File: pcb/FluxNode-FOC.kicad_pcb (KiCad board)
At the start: 2 copper layers, 5 parts, among them IC1 DRV8323SRTAR, J1 XT60PW-F, J2 XT60PW-M, Q1 TPW1R306PL, U1 STM32G474RET6

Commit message: Unified all different LCSC part numbers of the same exact components to just one variant
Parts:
- removed Q1: TPW1R306PL, FluxNode-FOC:SOP_ADVANCE
- added C101: 100nF X7R 50V, FluxNode-FOC:C_0402_1005_DensityHigh, F.Cu at (369.8, 91.0)
- added C102: 100nF X7R 50V, FluxNode-FOC:C_0402_1005_DensityHigh, F.Cu at (369.8, 92.8)
- added C103: 22uF X7R 10V, FluxNode-FOC:C_0805_2012_DensityHigh, F.Cu at (363.1, 90.2)
- added C104: 2u2 X7R 100V, FluxNode-FOC:C_0805_2012_DensityHigh, F.Cu at (363.1, 82.0)
- added C105: 2u2 100V, FluxNode-FOC:C_0805_2012_DensityHigh, F.Cu at (363.1, 84.7)
- added C106: 2u2 100V, FluxNode-FOC:C_0805_2012_DensityHigh, F.Cu at (363.1, 87.5)
- added C107: 100nF 100V, FluxNode-FOC:C_0603_1608_DensityHigh, F.Cu at (366.8, 89.4)
- added C108: 2u2 100V, FluxNode-FOC:C_0805_2012_DensityHigh, F.Cu at (492.1, 81.5)
- added C109: 2u2 100V, FluxNode-FOC:C_0805_2012_DensityHigh, F.Cu at (492.1, 84.3)
- added C110: 10u 25V, FluxNode-FOC:C_0805_2012_DensityHigh, F.Cu at (492.1, 87.0)
- added C111: 22uF X7R 10V, FluxNode-FOC:C_0805_2012_DensityHigh, F.Cu at (492.1, 89.8)
- added C112: 1uF X7R 10V, FluxNode-FOC:C_0402_1005_DensityHigh, F.Cu at (369.8, 89.2)
- added C113: 100nF X7R 50V, FluxNode-FOC:C_0402_1005_DensityHigh, F.Cu at (491.5, 92.1)
- added C114: 15uF 25V, FluxNode-FOC:C_1210_3225_DensityHigh, F.Cu at (462.4, 106.5)
- added C115: 15uF 25V, FluxNode-FOC:C_1210_3225_DensityHigh, F.Cu at (462.4, 110.3)
- added C116: 2u2 X7R 100V, FluxNode-FOC:C_0805_2012_DensityHigh, F.Cu at (363.1, 93.0)
- added C117: 2u2 100V, FluxNode-FOC:C_0805_2012_DensityHigh, F.Cu at (363.1, 95.7)
- added C118: 4u7 100V, FluxNode-FOC:C_1206_3216_DensityHigh, F.Cu at (367.5, 82.5)
- added C119: 4u7 100V, FluxNode-FOC:C_1206_3216_DensityHigh, F.Cu at (367.5, 86.3)
- added C120: 220n 100V, FluxNode-FOC:C_0603_1608_DensityHigh, F.Cu at (366.8, 91.7)
- added C121: 220n 100V, FluxNode-FOC:C_0603_1608_DensityHigh, F.Cu at (366.8, 93.9)
- added C122: 1u 25V, FluxNode-FOC:C_0603_1608_DensityHigh, F.Cu at (486.8, 105.7)
- added C123: 10n 100V, FluxNode-FOC:C_0402_1005_DensityHigh, F.Cu at (491.5, 93.9)
- added C124: 4.7u 16V, FluxNode-FOC:C_0603_1608_DensityHigh, F.Cu at (486.8, 108.0)
- added C125: 1u X7R 10V, FluxNode-FOC:C_0402_1005_DensityHigh, F.Cu at (369.8, 94.6)
- added C126: 4.7u 100V, FluxNode-FOC:C_1206_3216_DensityHigh, F.Cu at (462.4, 81.7)
- added C127: 4.7u 100V, FluxNode-FOC:C_1206_3216_DensityHigh, F.Cu at (462.4, 84.8)
- added C128: 4.7u 100V, FluxNode-FOC:C_1206_3216_DensityHigh, F.Cu at (462.4, 87.8)
- added C129: 4.7u 100V, FluxNode-FOC:C_1206_3216_DensityHigh, F.Cu at (462.4, 90.8)
- added C130: 4.7u 100V, FluxNode-FOC:C_1206_3216_DensityHigh, F.Cu at (462.4, 93.9)
- added C131: 4.7u 100V, FluxNode-FOC:C_1206_3216_DensityHigh, F.Cu at (462.4, 97.0)
- added C132: 4.7u 100V, FluxNode-FOC:C_1206_3216_DensityHigh, F.Cu at (462.4, 100.0)
- added C133: 4.7u 100V, FluxNode-FOC:C_1206_3216_DensityHigh, F.Cu at (462.4, 103.0)
- added C134: 4.7u 100V, FluxNode-FOC:C_1206_3216_DensityHigh, F.Cu at (467.4, 81.7)
- added C135: 4.7u 100V, FluxNode-FOC:C_1206_3216_DensityHigh, F.Cu at (467.4, 84.8)
- added C136: 4.7u 100V, FluxNode-FOC:C_1206_3216_DensityHigh, F.Cu at (467.4, 87.8)
- added C137: 4.7u 100V, FluxNode-FOC:C_1206_3216_DensityHigh, F.Cu at (467.4, 90.8)
- added C138: 4.7u 100V, FluxNode-FOC:C_1206_3216_DensityHigh, F.Cu at (467.4, 93.9)
- added C139: 4.7u 100V, FluxNode-FOC:C_1206_3216_DensityHigh, F.Cu at (467.4, 97.0)
- added C140: 4.7u 100V, FluxNode-FOC:C_1206_3216_DensityHigh, F.Cu at (467.4, 100.0)
- added C141: 4.7u 100V, FluxNode-FOC:C_1206_3216_DensityHigh, F.Cu at (467.4, 103.0)
- added C142: 4.7u 100V, FluxNode-FOC:C_1206_3216_DensityHigh, F.Cu at (472.5, 81.7)
- added C143: 4.7u 100V, FluxNode-FOC:C_1206_3216_DensityHigh, F.Cu at (472.5, 84.8)
- added C144: 4.7u 100V, FluxNode-FOC:C_1206_3216_DensityHigh, F.Cu at (472.5, 87.8)
- added C145: 4.7u 100V, FluxNode-FOC:C_1206_3216_DensityHigh, F.Cu at (472.5, 90.8)
- added C146: 4.7u 100V, FluxNode-FOC:C_1206_3216_DensityHigh, F.Cu at (472.5, 93.9)
- added C147: 4.7u 100V, FluxNode-FOC:C_1206_3216_DensityHigh, F.Cu at (472.5, 97.0)
- added C148: 4.7u 100V, FluxNode-FOC:C_1206_3216_DensityHigh, F.Cu at (472.5, 100.0)
- added C149: 4.7u 100V, FluxNode-FOC:C_1206_3216_DensityHigh, F.Cu at (472.5, 103.0)
- added C150: 4.7u 100V, FluxNode-FOC:C_1206_3216_DensityHigh, F.Cu at (477.6, 81.7)
- added C151: 4.7u 100V, FluxNode-FOC:C_1206_3216_DensityHigh, F.Cu at (477.6, 84.8)
- added C152: 4.7u 100V, FluxNode-FOC:C_1206_3216_DensityHigh, F.Cu at (477.6, 87.8)
- added C153: 4.7u 100V, FluxNode-FOC:C_1206_3216_DensityHigh, F.Cu at (477.6, 90.8)
- added C154: 4.7u 100V, FluxNode-FOC:C_1206_3216_DensityHigh, F.Cu at (477.6, 93.9)
- added C155: 4.7u 100V, FluxNode-FOC:C_1206_3216_DensityHigh, F.Cu at (477.6, 97.0)
- added C156: 4.7u 100V, FluxNode-FOC:C_1206_3216_DensityHigh, F.Cu at (477.6, 100.0)
- added C157: 4.7u 100V, FluxNode-FOC:C_1206_3216_DensityHigh, F.Cu at (477.6, 103.0)
- added C158: 4.7u 100V, FluxNode-FOC:C_1206_3216_DensityHigh, F.Cu at (482.6, 81.7)
- added C159: 4.7u 100V, FluxNode-FOC:C_1206_3216_DensityHigh, F.Cu at (482.6, 84.8)
- added C160: 4.7u 100V, FluxNode-FOC:C_1206_3216_DensityHigh, F.Cu at (482.6, 87.8)
- added C161: 4.7u 100V, FluxNode-FOC:C_1206_3216_DensityHigh, F.Cu at (482.6, 90.8)
- added C162: 4.7u 100V, FluxNode-FOC:C_1206_3216_DensityHigh, F.Cu at (482.6, 93.9)
- added C163: 4.7u 100V, FluxNode-FOC:C_1206_3216_DensityHigh, F.Cu at (482.6, 97.0)
- added C164: 4.7u 100V, FluxNode-FOC:C_1206_3216_DensityHigh, F.Cu at (482.6, 100.0)
- added C165: 4.7u 100V, FluxNode-FOC:C_1206_3216_DensityHigh, F.Cu at (482.6, 103.0)
- added C166: 4.7u 100V, FluxNode-FOC:C_1206_3216_DensityHigh, F.Cu at (487.6, 81.7)
- added C167: 4.7u 100V, FluxNode-FOC:C_1206_3216_DensityHigh, F.Cu at (487.6, 84.8)
- added C168: 4.7u 100V, FluxNode-FOC:C_1206_3216_DensityHigh, F.Cu at (487.6, 87.8)
- added C169: 4.7u 100V, FluxNode-FOC:C_1206_3216_DensityHigh, F.Cu at (487.6, 90.8)
- added C170: 4.7u 100V, FluxNode-FOC:C_1206_3216_DensityHigh, F.Cu at (487.6, 93.9)
- added C171: 4.7u 100V, FluxNode-FOC:C_1206_3216_DensityHigh, F.Cu at (487.6, 97.0)
- added C172: 4.7u 100V, FluxNode-FOC:C_1206_3216_DensityHigh, F.Cu at (487.6, 100.0)
- added C173: 4.7u 100V, FluxNode-FOC:C_1206_3216_DensityHigh, F.Cu at (487.6, 103.0)
- added C201: 1uF X7R 10V, FluxNode-FOC:C_0402_1005_DensityHigh, F.Cu at (444.2, 37.3)
- added C202: 100n 50V, FluxNode-FOC:C_0402_1005_DensityHigh, F.Cu at (444.2, 39.1)
- added C203: 100n 50V, FluxNode-FOC:C_0402_1005_DensityHigh, F.Cu at (444.2, 40.9)
- added C204: 100n 50V, FluxNode-FOC:C_0402_1005_DensityHigh, F.Cu at (444.2, 42.7)
- added C205: 100n 50V, FluxNode-FOC:C_0402_1005_DensityHigh, F.Cu at (444.2, 44.5)
- added C206: 4.7u 16V, FluxNode-FOC:C_0603_1608_DensityHigh, F.Cu at (449.8, 40.0)
- added C207: 1uF 10V, FluxNode-FOC:C_0402_1005_DensityHigh, F.Cu at (446.8, 37.3)
- added C208: 100n 50V, FluxNode-FOC:C_0402_1005_DensityHigh, F.Cu at (446.8, 39.1)
- added C209: 1uF X7R 10V, FluxNode-FOC:C_0402_1005_DensityHigh, F.Cu at (446.8, 40.9)
- added C210: 100n 50V, FluxNode-FOC:C_0402_1005_DensityHigh, F.Cu at (446.8, 42.7)
- added C211: 4.7u X5R 25V, FluxNode-FOC:C_0402_1005_DensityHigh, F.Cu at (446.8, 44.5)
- added C212: 1nF 25V, FluxNode-FOC:C_0402_1005_DensityHigh, F.Cu at (339.0, 138.9)
- added C213: 1nF 25V, FluxNode-FOC:C_0402_1005_DensityHigh, F.Cu at (339.0, 140.7)
- added C214: 1nF 25V, FluxNode-FOC:C_0402_1005_DensityHigh, F.Cu at (339.0, 142.5)
- added C215: 470pF 50V, FluxNode-FOC:C_0402_1005_DensityHigh, F.Cu at (365.4, -21.0)
- added C216: 470pF 50V, FluxNode-FOC:C_0402_1005_DensityHigh, F.Cu at (365.4, -19.2)
- added C217: 470pF 50V, FluxNode-FOC:C_0402_1005_DensityHigh, F.Cu at (365.4, -17.4)
- added C301: 1u 25V, FluxNode-FOC:C_0603_1608_DensityHigh, F.Cu at (490.2, 61.9)
- added C302: 4u7 100V, FluxNode-FOC:C_1206_3216_DensityHigh, F.Cu at (491.0, 59.2)
- added C303: 100nF 100V, FluxNode-FOC:C_0603_1608_DensityHigh, F.Cu at (490.2, 64.1)
- added C308: 100nF 50V, FluxNode-FOC:C_0402_1005_DensityHigh, F.Cu at (198.2, 45.1)
- added C309: 1uF 50V, FluxNode-FOC:C_0603_1608_DensityHigh, F.Cu at (125.5, 179.9)
- added C401: 100n 50V, FluxNode-FOC:C_0402_1005_DensityHigh, F.Cu at (268.2, 131.8)
- added C501: 100nF, FluxNode-FOC:C_0402_1005_DensityHigh, F.Cu at (318.8, 138.9)
- added C502: 100nF, FluxNode-FOC:C_0402_1005_DensityHigh, F.Cu at (318.8, 140.7)
- added C503: 100nF 50V, FluxNode-FOC:C_0402_1005_DensityHigh, F.Cu at (318.8, 142.5)
- added C504: 100nF 50V, FluxNode-FOC:C_0402_1005_DensityHigh, F.Cu at (318.8, 144.3)
- added C701: 1nF 1kV, FluxNode-FOC:C_0603_1608_DensityHigh, F.Cu at (256.0, 139.1)
- added C702: 1nF 1kV, FluxNode-FOC:C_0603_1608_DensityHigh, F.Cu at (256.0, 141.4)
- added C703: 1nF 1kV, FluxNode-FOC:C_0603_1608_DensityHigh, F.Cu at (256.0, 143.6)
- added C704: 1nF 1kV, FluxNode-FOC:C_0603_1608_DensityHigh, F.Cu at (256.0, 145.9)
- added C801: 3n3 10% 100V, FluxNode-FOC:C_0402_1005_DensityHigh, F.Cu at (357.1, -3.63)
- added C802: 3n3 10% 100V, FluxNode-FOC:C_0402_1005_DensityHigh, F.Cu at (357.1, -1.83)
- added C803: 4.7u 100V, FluxNode-FOC:C_1206_3216_DensityHigh, F.Cu at (339.8, -11.9)
- added C804: 100nF 100V, FluxNode-FOC:C_1206_3216_DensityHigh, F.Cu at (339.8, -8.80)
- added C805: 3n3 10% 100V, FluxNode-FOC:C_0402_1005_DensityHigh, F.Cu at (357.1, -0.03)
- added C806: 3n3 10% 100V, FluxNode-FOC:C_0402_1005_DensityHigh, F.Cu at (357.1, 1.77)
- added C807: 100nF 100V, FluxNode-FOC:C_1206_3216_DensityHigh, F.Cu at (339.8, -5.75)
- added C808: 4.7u 100V, FluxNode-FOC:C_1206_3216_DensityHigh, F.Cu at (339.8, -2.71)
- added C809: 3n3 10% 100V, FluxNode-FOC:C_0402_1005_DensityHigh, F.Cu at (357.1, 3.57)
- added C810: 3n3 10% 100V, FluxNode-FOC:C_0402_1005_DensityHigh, F.Cu at (357.1, 5.37)
- added C811: 100nF 100V, FluxNode-FOC:C_1206_3216_DensityHigh, F.Cu at (339.8, 0.34)
- added C812: 4.7u 100V, FluxNode-FOC:C_1206_3216_DensityHigh, F.Cu at (339.8, 3.40)
- added D101: SMBJ51CD-M3_H, FluxNode-FOC:DIOM4336X24N, F.Cu at (433.9, 90.5)
- added D102: SMBJ51CD-M3_H, FluxNode-FOC:DIOM4336X24N, F.Cu at (433.9, 95.5)
- added D501: PESD4USB3U-TBSX, FluxNode-FOC:PESD4USB3UTBSX, F.Cu at (328.1, 150.3)
- added D801: BAT41ZFILM, FluxNode-FOC:SOD3816X145N, F.Cu at (334.4, -20.0)
- added D802: BAT41ZFILM, FluxNode-FOC:SOD3816X145N, F.Cu at (334.4, -16.7)
- added D803: BAT41ZFILM, FluxNode-FOC:SOD3816X145N, F.Cu at (334.4, -13.4)
- added D804: BAT41ZFILM, FluxNode-FOC:SOD3816X145N, F.Cu at (334.4, -10.2)
- added D805: BAT41ZFILM, FluxNode-FOC:SOD3816X145N, F.Cu at (334.4, -6.88)
- added D806: BAT41ZFILM, FluxNode-FOC:SOD3816X145N, F.Cu at (334.4, -3.60)
- added D807: BAT41ZFILM, FluxNode-FOC:SOD3816X145N, F.Cu at (334.4, -0.32)
- added D808: BAT41ZFILM, FluxNode-FOC:SOD3816X145N, F.Cu at (334.4, 2.96)
- added D809: BAT41ZFILM, FluxNode-FOC:SOD3816X145N, F.Cu at (334.4, 6.24)
- added FB101: 1k @ 100MHz, FluxNode-FOC:R_0805_2012_DensityHigh, F.Cu at (466.8, 105.8)
- added FB102: 1k @ 100MHz, FluxNode-FOC:R_0805_2012_DensityHigh, F.Cu at (466.8, 111.0)
- added FB103: 1k @ 100MHz, FluxNode-FOC:R_0805_2012_DensityHigh, F.Cu at (466.8, 108.4)
- added FB201: 1k @ 100MHz, FluxNode-FOC:R_0805_2012_DensityHigh, F.Cu at (450.0, 37.6)
- added FID701: Fiducial, Fiducial:Fiducial_1mm_Mask2mm, F.Cu at (256.0, 132.7)
- added FID702: Fiducial, Fiducial:Fiducial_1mm_Mask2mm, F.Cu at (256.0, 136.2)
- added FID703: Fiducial, Fiducial:Fiducial_1mm_Mask2mm, F.Cu at (259.6, 132.7)
- added FID704: Fiducial, Fiducial:Fiducial_1mm_Mask2mm, F.Cu at (259.6, 136.2)
- added FID705: Fiducial, Fiducial:Fiducial_1mm_Mask2mm, F.Cu at (263.1, 132.7)
- added FID706: Fiducial, Fiducial:Fiducial_1mm_Mask2mm, F.Cu at (263.1, 136.2)
- added H701: MountingHole_Pad, MountingHole:MountingHole_3.2mm_M3_Pad_Via, F.Cu at (250.3, 134.9)
- added H702: MountingHole_Pad, MountingHole:MountingHole_3.2mm_M3_Pad_Via, F.Cu at (250.3, 142.8)
- added H703: MountingHole_Pad, MountingHole:MountingHole_3.2mm_M3_Pad_Via, F.Cu at (250.3, 150.8)
- added H704: MountingHole_Pad, MountingHole:MountingHole_3.2mm_M3_Pad_Via, F.Cu at (250.3, 158.7)
- added J501: XT30PW_2_2_-M.G.B, FluxNode-FOC:AMASS_XT30PW_2_2_-M.G.B, F.Cu at (164.7, 164.9)
- added J502: Conn_01x08_Pin, Connector_JST:JST_GH_SM08B-GHS-TB_1x08-1MP_P1.25mm_Horizontal, F.Cu at (70.9, 127.5)
- added J503: TYPE-C-31-M-12, FluxNode-FOC:HRO_TYPE-C-31-M-12, F.Cu at (326.2, 144.7)
- added L101: 22uH 830mA 360mOhms, FluxNode-FOC:L_Coilcraft_LPS4018, F.Cu at (373.0, 83.3)
- added L102: 2.2uH 1,2A 100mOhms, FluxNode-FOC:L_Coilcraft_LPS3314, F.Cu at (477.2, 107.2)
- added L103: 22uH 830mA 360mOhms, FluxNode-FOC:L_Coilcraft_LPS4018, F.Cu at (471.6, 107.3)
- added Q301: TPW1R306PL, FluxNode-FOC:SOP_ADVANCE, F.Cu at (151.7, 167.1)
- added Q801: TPW1R306PL, FluxNode-FOC:SOP_ADVANCE, F.Cu at (385.1, 109.8)
- added Q802: TPW1R306PL, FluxNode-FOC:SOP_ADVANCE, F.Cu at (391.2, 109.8)
- added Q803: TPW1R306PL, FluxNode-FOC:SOP_ADVANCE, F.Cu at (340.4, -17.9)
- added Q804: TPW1R306PL, FluxNode-FOC:SOP_ADVANCE, F.Cu at (346.6, -17.9)
- added Q805: TPW1R306PL, FluxNode-FOC:SOP_ADVANCE, F.Cu at (352.8, -17.9)
- added Q806: TPW1R306PL, FluxNode-FOC:SOP_ADVANCE, F.Cu at (359.0, -17.9)
- added R101: 10k 1% 50V, FluxNode-FOC:R_0402_1005_DensityHigh, F.Cu at (368.0, 63.3)
- added R102: 0R, FluxNode-FOC:R_0402_1005_DensityHigh, F.Cu at (368.0, 61.5)
- added R103: 100k 1% 50V, FluxNode-FOC:R_0402_1005_DensityHigh, F.Cu at (368.0, 65.1)
- added R104: 9.09k 1% 50V, FluxNode-FOC:R_0402_1005_DensityHigh, F.Cu at (491.5, 101.1)
- added R201: 22R 1%, FluxNode-FOC:R_0402_1005_DensityHigh, F.Cu at (339.0, 144.3)
- added R202: 22R 1%, FluxNode-FOC:R_0402_1005_DensityHigh, F.Cu at (339.0, 146.1)
- added R203: 22R 1%, FluxNode-FOC:R_0402_1005_DensityHigh, F.Cu at (339.0, 147.9)
- added R204: 22R 1%, FluxNode-FOC:R_0402_1005_DensityHigh, F.Cu at (339.0, 149.7)
- added R205: 22R 1%, FluxNode-FOC:R_0402_1005_DensityHigh, F.Cu at (339.0, 151.5)
- added R206: 1K 1%, FluxNode-FOC:R_0402_1005_DensityHigh, F.Cu at (365.4, -15.6)
- added R207: 1K 1%, FluxNode-FOC:R_0402_1005_DensityHigh, F.Cu at (365.4, -13.8)
- added R208: 1K 1%, FluxNode-FOC:R_0402_1005_DensityHigh, F.Cu at (365.4, -12.0)
- added R304: 100, FluxNode-FOC:R_0402_1005_DensityHigh, F.Cu at (198.2, 46.9)
- added R305: 10k, FluxNode-FOC:R_0402_1005_DensityHigh, F.Cu at (198.2, 48.7)
- added R306: 4.7, FluxNode-FOC:R_0603_1608_DensityHigh, F.Cu at (153.7, 171.9)
- added R307: 1.5, FluxNode-FOC:R_0603_1608_DensityHigh, F.Cu at (152.4, 171.9)
- added R308: 47k, FluxNode-FOC:R_0402_1005_DensityHigh, F.Cu at (198.2, 50.5)
- added R401: 100k 1%, FluxNode-FOC:R_0402_1005_DensityHigh, F.Cu at (268.2, 133.6)
- added R402: 8k2 1%, FluxNode-FOC:R_0402_1005_DensityHigh, F.Cu at (268.2, 135.4)
- added R501: 5k1 1%, FluxNode-FOC:R_0402_1005_DensityHigh, F.Cu at (318.8, 146.1)
- added R502: 5k1 1%, FluxNode-FOC:R_0402_1005_DensityHigh, F.Cu at (318.8, 147.9)
- added R503: 100k, FluxNode-FOC:R_0402_1005_DensityHigh, F.Cu at (318.8, 149.7)
- added R504: 100k, FluxNode-FOC:R_0402_1005_DensityHigh, F.Cu at (318.8, 151.5)
- added R701: 0R, FluxNode-FOC:R_0603_1608_DensityHigh, F.Cu at (259.3, 139.1)
- added R702: 0R, FluxNode-FOC:R_0603_1608_DensityHigh, F.Cu at (259.3, 141.2)
- added R703: 0R, FluxNode-FOC:R_0603_1608_DensityHigh, F.Cu at (259.3, 143.4)
- added R704: 0R, FluxNode-FOC:R_0603_1608_DensityHigh, F.Cu at (259.3, 145.5)
- added R801: 7.5 1% 0.5W, FluxNode-FOC:R_0805_2012_DensityHigh, F.Cu at (353.9, -12.1)
- added R802: 7.5 1% 0.5W, FluxNode-FOC:R_0805_2012_DensityHigh, F.Cu at (353.9, -9.55)
- added R803: 5R 1% 0.4W, FluxNode-FOC:R_0603_1608_DensityHigh, F.Cu at (343.9, -12.3)
- added R804: 5R 1% 0.4W, FluxNode-FOC:R_0603_1608_DensityHigh, F.Cu at (343.9, -10.2)
- added R805: 0.5m 1% 2W, FluxNode-FOC:R_1206_3216_DensityHigh, F.Cu at (358.2, -11.9)
- added R806: 43k 1% 75V, FluxNode-FOC:R_0603_1608_DensityHigh, F.Cu at (343.9, -8.01)
- added R807: 43k 1% 75V, FluxNode-FOC:R_0603_1608_DensityHigh, F.Cu at (343.9, -5.86)
- added R808: 6k8 1% 75V, FluxNode-FOC:R_0603_1608_DensityHigh, F.Cu at (343.9, -3.71)
- added R809: 43k 1% 75V, FluxNode-FOC:R_0603_1608_DensityHigh, F.Cu at (343.9, -1.55)
- added R810: 43k 1% 75V, FluxNode-FOC:R_0603_1608_DensityHigh, F.Cu at (347.1, -12.3)
- added R811: 6k8 1% 75V, FluxNode-FOC:R_0603_1608_DensityHigh, F.Cu at (347.1, -10.2)
- added R812: 43k 1% 75V, FluxNode-FOC:R_0603_1608_DensityHigh, F.Cu at (347.1, -8.01)
- added R813: 43k 1% 75V, FluxNode-FOC:R_0603_1608_DensityHigh, F.Cu at (347.1, -5.86)
- added R814: 6k8 1% 75V, FluxNode-FOC:R_0603_1608_DensityHigh, F.Cu at (347.1, -3.71)
- added R815: 7.5 1% 0.5W, FluxNode-FOC:R_0805_2012_DensityHigh, F.Cu at (353.9, -7.00)
- added R816: 7.5 1% 0.5W, FluxNode-FOC:R_0805_2012_DensityHigh, F.Cu at (353.9, -4.46)
- added R817: 0.5m 1% 2W, FluxNode-FOC:R_1206_3216_DensityHigh, F.Cu at (358.2, -8.96)
- added R818: 5R 1% 0.4W, FluxNode-FOC:R_0603_1608_DensityHigh, F.Cu at (347.1, -1.55)
- added R819: 5R 1% 0.4W, FluxNode-FOC:R_0603_1608_DensityHigh, F.Cu at (350.4, -12.3)
- added R820: 7.5 1% 0.5W, FluxNode-FOC:R_0805_2012_DensityHigh, F.Cu at (353.9, -1.91)
- added R821: 7.5 1% 0.5W, FluxNode-FOC:R_0805_2012_DensityHigh, F.Cu at (353.9, 0.65)
- added R822: 0.5m 1% 2W, FluxNode-FOC:R_1206_3216_DensityHigh, F.Cu at (358.2, -6.00)
- added R823: 5R 1% 0.4W, FluxNode-FOC:R_0603_1608_DensityHigh, F.Cu at (350.4, -10.2)
- added R824: 5R 1% 0.4W, FluxNode-FOC:R_0603_1608_DensityHigh, F.Cu at (350.4, -8.01)
- added U101: TPS62172DSG, Package_SON:WSON-8-1EP_2x2mm_P0.5mm_EP0.9x1.6mm_ThermalVias, F.Cu at (490.7, 106.5)
- added U102: LMR36506MSC5RPERQ1, FluxNode-FOC:LMR36503, F.Cu at (373.0, 94.9)
- added U103: LP2992IM5-3.3/NOPB, Package_TO_SOT_SMD:SOT-23-5, F.Cu at (482.4, 107.0)
- added U104: LMR36006FSCQ, FluxNode-FOC:LMR36006, F.Cu at (372.9, 90.6)
- added U301: UCC27511ADBV, Package_TO_SOT_SMD:SOT-23-6, F.Cu at (153.3, 175.2)
- added U501: USBLC6-2SC6, Package_TO_SOT_SMD:SOT-23-6, F.Cu at (322.7, 150.5)
- moved IC1 255.8 mm to (386.6, 56.4)
- moved U201 251.8 mm to (386.5, 69.6)
- moved J102 5.83 mm to (104.4, 69.7)
- moved J101 5.50 mm to (95.3, 69.7)
- renumbered J1 to J101, J2 to J102, U1 to U201
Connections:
- net /03-Motor-Driver/SHA renamed /03 Motor Control - Gate Driver/SHA
- net /03-Motor-Driver/SHB renamed /03 Motor Control - Gate Driver/SHB
- net /03-Motor-Driver/SHC renamed /03 Motor Control - Gate Driver/SHC
- net /03-Motor-Driver/SNA renamed /03 Motor Control - Gate Driver/SNA
- net /03-Motor-Driver/SNB renamed /03 Motor Control - Gate Driver/SNB
- net /03-Motor-Driver/SNC renamed /03 Motor Control - Gate Driver/SNC
- net /03-Motor-Driver/SPA renamed /03 Motor Control - Gate Driver/SPA
- net /03-Motor-Driver/SPB renamed /03 Motor Control - Gate Driver/SPB
- net /03-Motor-Driver/SPC renamed /03 Motor Control - Gate Driver/SPC
- IC1 pad 1: unconnected-(IC1-CPL-Pad1) -> Net-(IC1-CPL)
- IC1 pad 13: /03-Motor-Driver/GLB -> /03 Motor Control - Gate Driver/GLB
- IC1 pad 15: /03-Motor-Driver/GHB -> /03 Motor Control - Gate Driver/GHB
- IC1 pad 16: /03-Motor-Driver/GHC -> /03 Motor Control - Gate Driver/GHC
- IC1 pad 18: /03-Motor-Driver/GLC -> /03 Motor Control - Gate Driver/GLC
- IC1 pad 2: unconnected-(IC1-CPH-Pad2) -> Net-(IC1-CPH)
- IC1 pad 21: /03-Motor-Driver/SOC -> /02 MCU/SOC
- IC1 pad 22: /03-Motor-Driver/SOB -> /02 MCU/SOB
- IC1 pad 23: /03-Motor-Driver/SOA -> /02 MCU/SOA
- IC1 pad 24: /03-Motor-Driver/VREF -> +A3V3
- IC1 pad 25: /03-Motor-Driver/nFault -> /02 MCU/DRV_nFAULT
- IC1 pad 26: /03-Motor-Driver/SDO -> /02 MCU/SPI1_MISO
- IC1 pad 27: /03-Motor-Driver/SDI -> /02 MCU/SPI1_MOSI
- IC1 pad 28: /03-Motor-Driver/SCLK -> /02 MCU/SPI1_SCK
- IC1 pad 29: /03-Motor-Driver/nSCS -> /02 MCU/SPI1_DRV_CS
- IC1 pad 3: unconnected-(IC1-VCP-Pad3) -> Net-(IC1-VCP)
- IC1 pad 30: /03-Motor-Driver/EN -> /02 MCU/DRV_EN
- IC1 pad 31: /03-Motor-Driver/CAL -> /02 MCU/DRV_CAL
- IC1 pad 32: unconnected-(IC1-AGND-Pad32) -> GND
- IC1 pad 33: unconnected-(IC1-DVDD-Pad33) -> Net-(IC1-DVDD)
- IC1 pad 34: /03-Motor-Driver/INHA -> /02 MCU/DRV_PWM_HA
- IC1 pad 35: /03-Motor-Driver/INLA -> /02 MCU/DRV_PWM_LA
- IC1 pad 36: /03-Motor-Driver/INHB -> /02 MCU/DRV_PWM_HB
- IC1 pad 37: /03-Motor-Driver/INLB -> /02 MCU/DRV_PWM_LB
- IC1 pad 38: /03-Motor-Driver/INHC -> /02 MCU/DRV_PWM_HC
- IC1 pad 39: /03-Motor-Driver/INLC -> /02 MCU/DRV_PWM_LC
- IC1 pad 4: unconnected-(IC1-VM-Pad4) -> +VBAT
- IC1 pad 40: unconnected-(IC1-PGND-Pad40) -> GND
- IC1 pad 41: unconnected-(IC1-EP-Pad41) -> GND
- IC1 pad 5: unconnected-(IC1-VDRAIN-Pad5) -> +VBAT
- IC1 pad 6: /03-Motor-Driver/GHA -> /03 Motor Control - Gate Driver/GHA
- IC1 pad 8: /03-Motor-Driver/GLA -> /03 Motor Control - Gate Driver/GLA
- J101 pad 2: /01-Power/+VBAT -> +VBAT
- J102 pad 2: /01-Power/+VBAT -> +VBAT
- U201 pad 1: unconnected-(U1-VBAT-Pad1) -> +3V3
- U201 pad 10: unconnected-(U1-PC2-Pad10) -> /02 MCU/DRV_PWM_HA
- U201 pad 11: unconnected-(U1-PC3-Pad11) -> /02 MCU/SENSE_UA
- U201 pad 12: unconnected-(U1-PA0-Pad12) -> /02 MCU/SENSE_UC
- U201 pad 13: unconnected-(U1-PA1-Pad13) -> /02 MCU/SENSE_UB
- U201 pad 14: unconnected-(U1-PA2-Pad14) -> /02 MCU/DRV_CAL
- U201 pad 15: Net-(U1-VSS-Pad15) -> GND
- U201 pad 16: unconnected-(U1-VDD-Pad16) -> +3V3
- U201 pad 17: unconnected-(U1-PA3-Pad17) -> /02 MCU/DRV_EN
- U201 pad 18: unconnected-(U1-PA4-Pad18) -> /02 MCU/SPI1_DRV_CS
- U201 pad 19: unconnected-(U1-PA5-Pad19) -> /02 MCU/SPI1_SCK
- U201 pad 2: unconnected-(U1-PC13-Pad2) -> /02 MCU/DRV_PWM_LC
- U201 pad 20: unconnected-(U1-PA6-Pad20) -> /02 MCU/SPI1_MISO
- U201 pad 21: unconnected-(U1-PA7-Pad21) -> /02 MCU/SPI1_MOSI
- U201 pad 22: unconnected-(U1-PC4-Pad22) -> /02 MCU/DRV_nFAULT
- U201 pad 23: unconnected-(U1-PC5-Pad23) -> /02 MCU/SPI1_MAG_CS
- U201 pad 24: unconnected-(U1-PB0-Pad24) -> /02 MCU/DRV_SOA_FILT
- U201 pad 25: unconnected-(U1-PB1-Pad25) -> /02 MCU/DRV_SOB_FILT
- U201 pad 26: unconnected-(U1-PB2-Pad26) -> /02 MCU/DRV_SOC_FILT
- U201 pad 27: unconnected-(U1-VSSA-Pad27) -> GND
- U201 pad 28: unconnected-(U1-VREF+-Pad28) -> /02 MCU/F_A3V3
- U201 pad 29: unconnected-(U1-VDDA-Pad29) -> /02 MCU/F_A3V3
- U201 pad 31: Net-(U1-VSS-Pad15) -> GND
- U201 pad 32: unconnected-(U1-VDD-Pad32) -> +3V3
- U201 pad 33: unconnected-(U1-PB11-Pad33) -> /02 MCU/FAN_CTRL
- U201 pad 34: unconnected-(U1-PB12-Pad34) -> /02 MCU/SENSE_TEMP_BRAKE
- U201 pad 35: unconnected-(U1-PB13-Pad35) -> /02 MCU/SENSE_VBAT
- U201 pad 36: unconnected-(U1-PB14-Pad36) -> /02 MCU/DRV_PWM_LB
- U201 pad 37: unconnected-(U1-PB15-Pad37) -> /02 MCU/USB_VBUS_SENSE
- U201 pad 41: unconnected-(U1-PC9-Pad41) -> /02 MCU/BRAKE_CTRL
- U201 pad 42: unconnected-(U1-PA8-Pad42) -> /02 MCU/SENSE_TEMP_FET
- U201 pad 43: unconnected-(U1-PA9-Pad43) -> /02 MCU/SENSE_TEMP_MOT
- U201 pad 45: unconnected-(U1-PA11-Pad45) -> /02 MCU/USB_D-
- U201 pad 46: unconnected-(U1-PA12-Pad46) -> /02 MCU/USB_D+
- U201 pad 47: Net-(U1-VSS-Pad15) -> GND
- U201 pad 48: unconnected-(U1-VDD-Pad48) -> +3V3
- U201 pad 49: unconnected-(U1-PA13-Pad49) -> /02 MCU/SWDIO
- U201 pad 5: unconnected-(U1-PF0-Pad5) -> /02 MCU/OSC_IN
- U201 pad 50: unconnected-(U1-PA14-Pad50) -> /02 MCU/SWCLK
- U201 pad 52: unconnected-(U1-PC10-Pad52) -> /02 MCU/AUX1_SPI3_CLK
- U201 pad 53: unconnected-(U1-PC11-Pad53) -> /02 MCU/AUX1_SPI3_MISO
- U201 pad 54: unconnected-(U1-PC12-Pad54) -> /02 MCU/AUX1_SPI3_MOSI
- U201 pad 56: unconnected-(U1-PB3-Pad56) -> /02 MCU/SWO
- U201 pad 58: unconnected-(U1-PB5-Pad58) -> /02 MCU/FDCAN_RX
- U201 pad 59: unconnected-(U1-PB6-Pad59) -> /02 MCU/FDCAN_TX
- U201 pad 6: unconnected-(U1-PF1-Pad6) -> /02 MCU/OSC_OUT
- U201 pad 60: unconnected-(U1-PB7-Pad60) -> /02 MCU/AUX1_I2C_SDA
- U201 pad 61: unconnected-(U1-PB8-Pad61) -> /02 MCU/AUX1_I2C_SCL
- U201 pad 62: unconnected-(U1-PB9-Pad62) -> /02 MCU/DRV_PWM_LA
- U201 pad 63: Net-(U1-VSS-Pad15) -> GND
- U201 pad 64: unconnected-(U1-VDD-Pad64) -> +3V3
- U201 pad 7: unconnected-(U1-PG10-Pad7) -> /02 MCU/NRST
- U201 pad 8: unconnected-(U1-PC0-Pad8) -> /02 MCU/DRV_PWM_HC
- U201 pad 9: unconnected-(U1-PC1-Pad9) -> /02 MCU/DRV_PWM_HB
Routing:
- net /02 MCU/DRV_PWM_LB: track 0.00 -> 18.2 mm, vias 0 -> 2
- net /02 MCU/SENSE_VBAT: track 0.00 -> 18.0 mm
- net /02 MCU/DRV_PWM_LA: track 0.00 -> 14.7 mm, vias 0 -> 2
- net /02 MCU/DRV_PWM_LC: track 0.00 -> 13.5 mm
- net /02 MCU/DRV_PWM_HC: track 0.00 -> 9.46 mm
- net /02 MCU/USB_VBUS_SENSE: track 0.00 -> 9.16 mm
- net /02 MCU/AUX1_I2C_SDA: track 0.00 -> 9.02 mm
- net /02 MCU/AUX1_I2C_SCL: track 0.00 -> 8.67 mm
- net /02 MCU/DRV_PWM_HB: track 0.00 -> 8.34 mm
- net /02 MCU/DRV_PWM_HA: track 0.00 -> 7.51 mm
- net /02 MCU/SWDIO: track 0.00 -> 7.20 mm
- net /02 MCU/SPI1_MOSI: track 0.00 -> 6.87 mm, vias 0 -> 2
- net /02 MCU/DRV_nFAULT: track 0.00 -> 6.87 mm
- net /02 MCU/FDCAN_TX: track 0.00 -> 6.74 mm
- net /02 MCU/SWCLK: track 0.00 -> 6.49 mm
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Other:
- board outline added: 69.7 x 76.7 mm

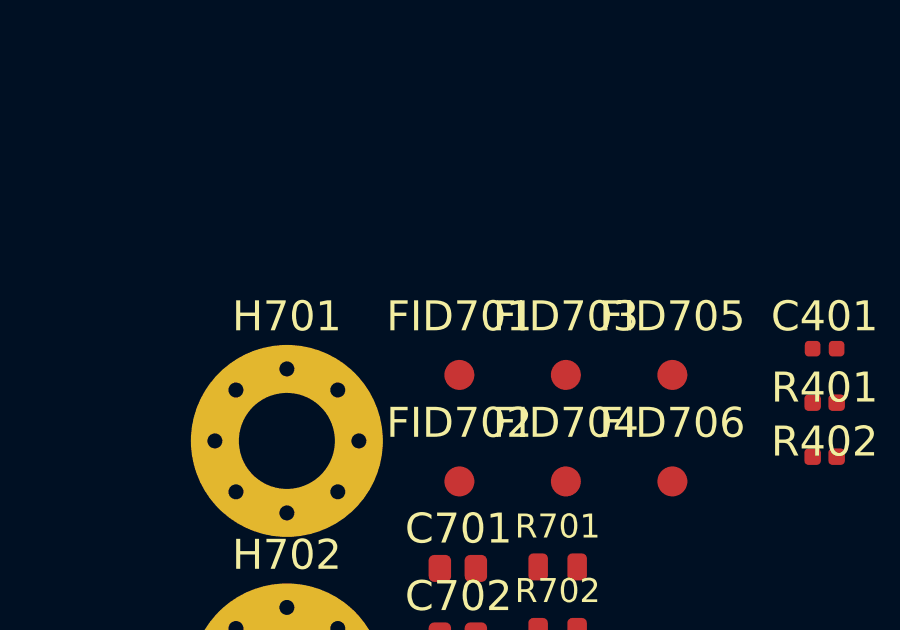
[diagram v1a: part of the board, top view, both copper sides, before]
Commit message: Some minor changes to the annotations
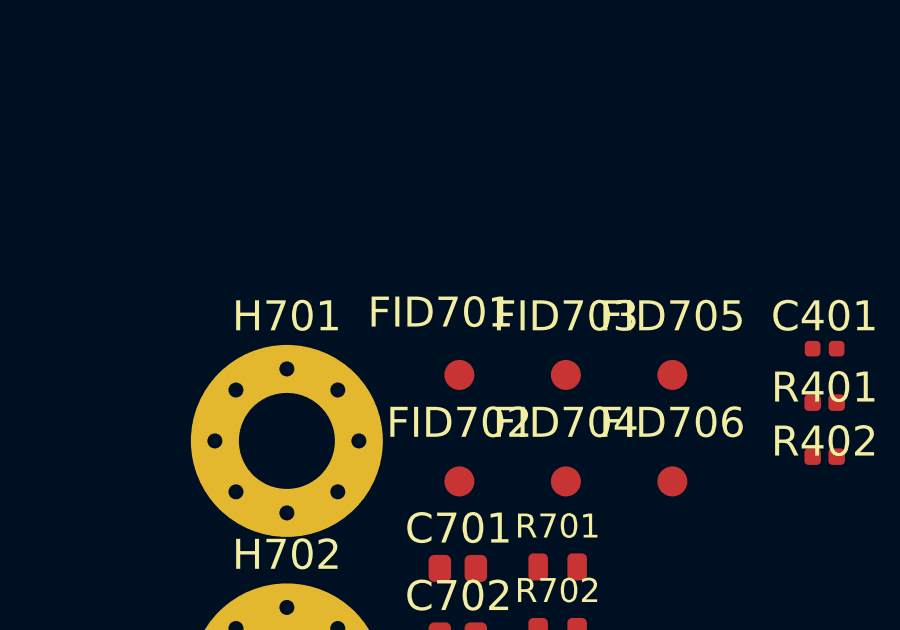
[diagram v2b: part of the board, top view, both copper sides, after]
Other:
- copper layers 2 -> 6
